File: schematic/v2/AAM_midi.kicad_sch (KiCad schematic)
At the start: 3 parts, among them J21 USB_A

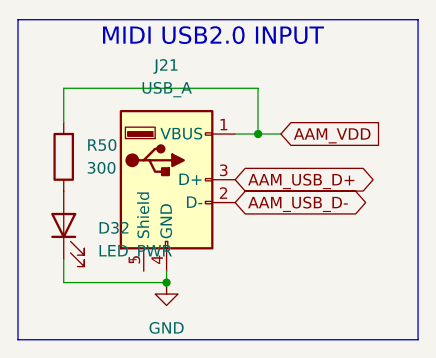
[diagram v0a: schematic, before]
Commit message: progress on putting things in different sheets
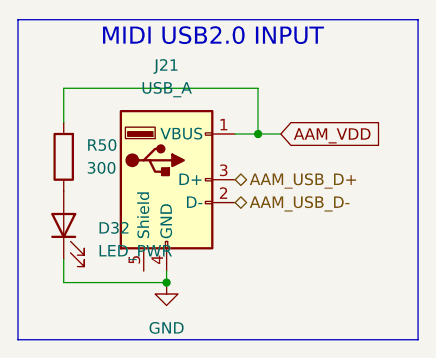
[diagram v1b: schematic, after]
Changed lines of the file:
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@@
-		)
-	)
-	(global_label "AAM_USB_D-"
-		(shape bidirectional)
-		(at 146.05 100.33 0)
-		(fields_autoplaced yes)
-		(effects
-			(font
-				(size 1.27 1.27)
-			)
-			(justify left)
-		)
-		(property "Intersheetrefs" "${INTERSHEET_REFS}"
-			(at 162.3627 100.33 0)
-			(effects
-				(font
-					(size 1.27 1.27)
-				)
-				(justify left)
-				(hide yes)
-			)
-		)
-	)
-	(global_label "AAM_USB_D+"
-		(shape bidirectional)
-		(at 146.05 97.79 0)
-		(fields_autoplaced yes)
-		(effects
-			(font
-				(size 1.27 1.27)
-			)
-			(justify left)
-		)
-		(property "Intersheetrefs" "${INTERSHEET_REFS}"
-			(at 162.3627 97.79 0)
-			(effects
-				(font
-					(size 1.27 1.27)
-				)
-				(justify left)
-				(hide yes)
-			)
 		)
 	)
@@
 		)
 	)
+	(hierarchical_label "AAM_USB_D+"
+		(shape bidirectional)
+		(at 146.05 97.79 0)
+		(effects
+			(font
+				(size 1.27 1.27)
+			)
+			(justify left)
+		)
+	)
+	(hierarchical_label "AAM_USB_D-"
+		(shape bidirectional)
+		(at 146.05 100.33 0)
+		(effects
+			(font
+				(size 1.27 1.27)
+			)
+			(justify left)
+		)
+	)

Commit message: v2 updates. remove sniffer
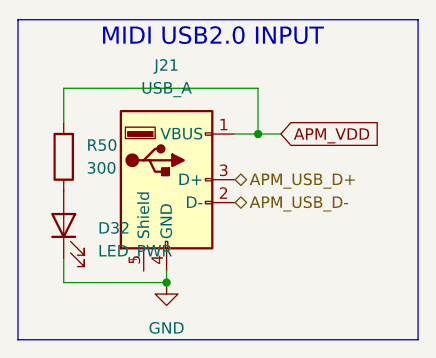
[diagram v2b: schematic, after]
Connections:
- net AAM_USB_D+ renamed APM_USB_D+
- net AAM_USB_D- renamed APM_USB_D-
- net AAM_VDD renamed APM_VDD
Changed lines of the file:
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@@
 		)
 	)
-	(global_label "AAM_VDD"
+	(global_label "APM_VDD"
 		(shape input)
 		(at 151.13 92.71 0)
@@
 		)
 	)
-	(hierarchical_label "AAM_USB_D+"
+	(hierarchical_label "APM_USB_D+"
 		(shape bidirectional)
 		(at 146.05 97.79 0)
@@
 		)
 	)
-	(hierarchical_label "AAM_USB_D-"
+	(hierarchical_label "APM_USB_D-"
 		(shape bidirectional)
 		(at 146.05 100.33 0)
